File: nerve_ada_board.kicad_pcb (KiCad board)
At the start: 4 copper layers, 120 x 120 mm, 64 parts, among them J10 CAN1, J11 CAN2, J2 TC2050-IDC, J3 2171750001, J5 WS2812B, J6 Camera, J7 PA4-7, J8 PC1-3, J9 PB4-5, SW1 SPST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

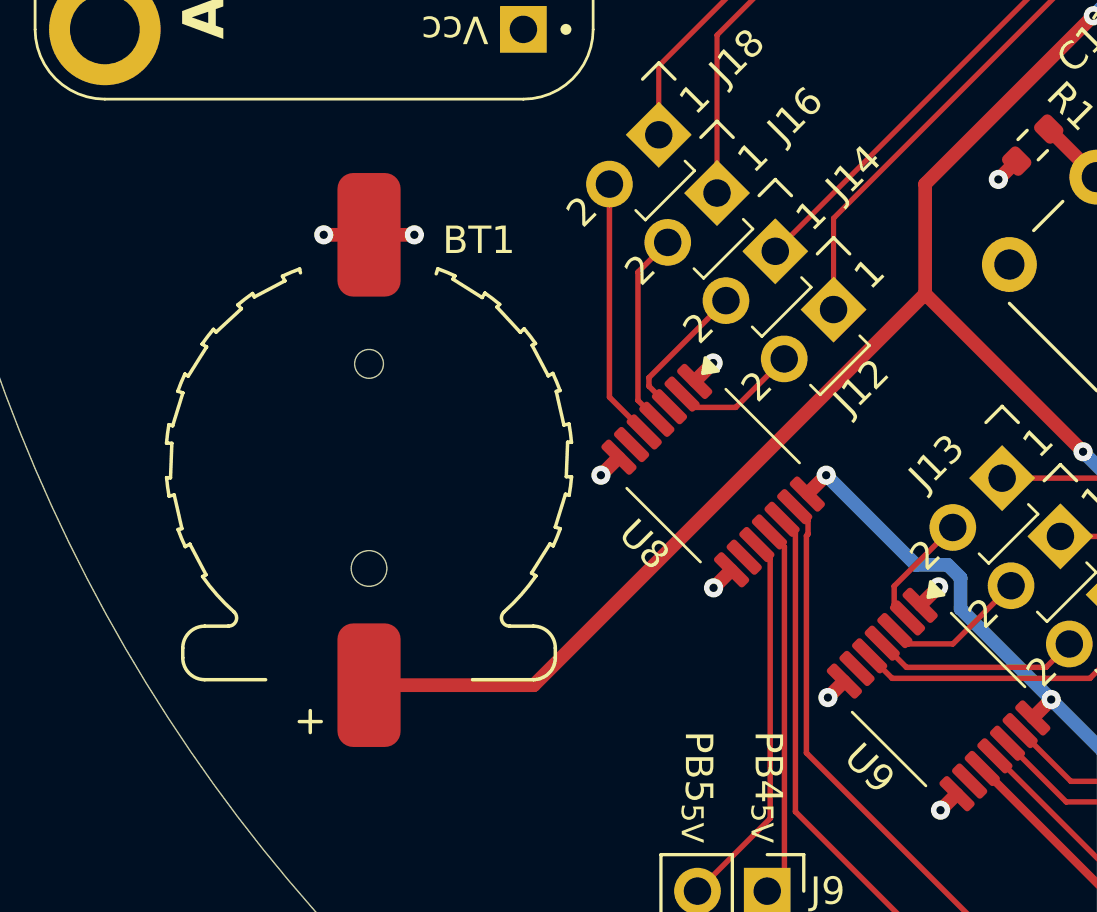
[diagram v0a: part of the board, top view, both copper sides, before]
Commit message: Update CR1220 battery holder component
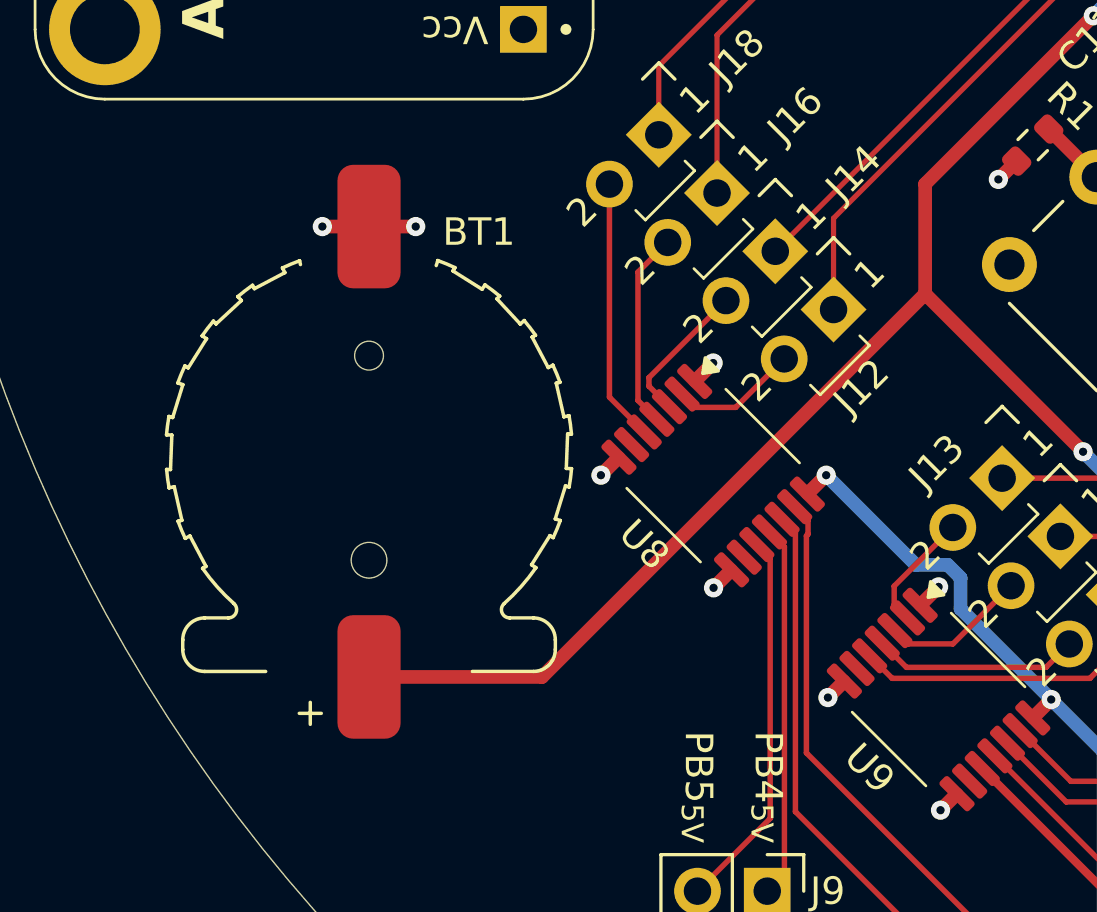
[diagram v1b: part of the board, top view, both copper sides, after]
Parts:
- BT1: footprint common:harwin_s8411-45r_cr1220_coin_battery_cell -> common:harwin_s8411-45r_cr1220
- moved BT1 0.30 mm to (105.5, 128.0)

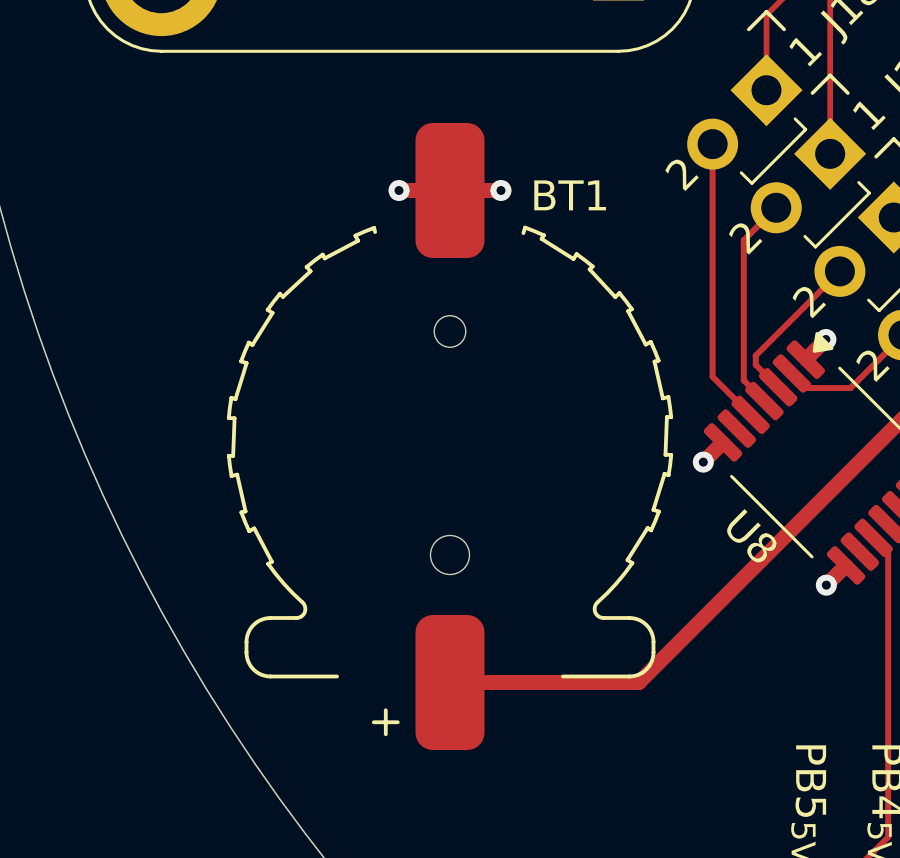
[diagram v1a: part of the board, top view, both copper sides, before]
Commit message: Update CR1220 component, again
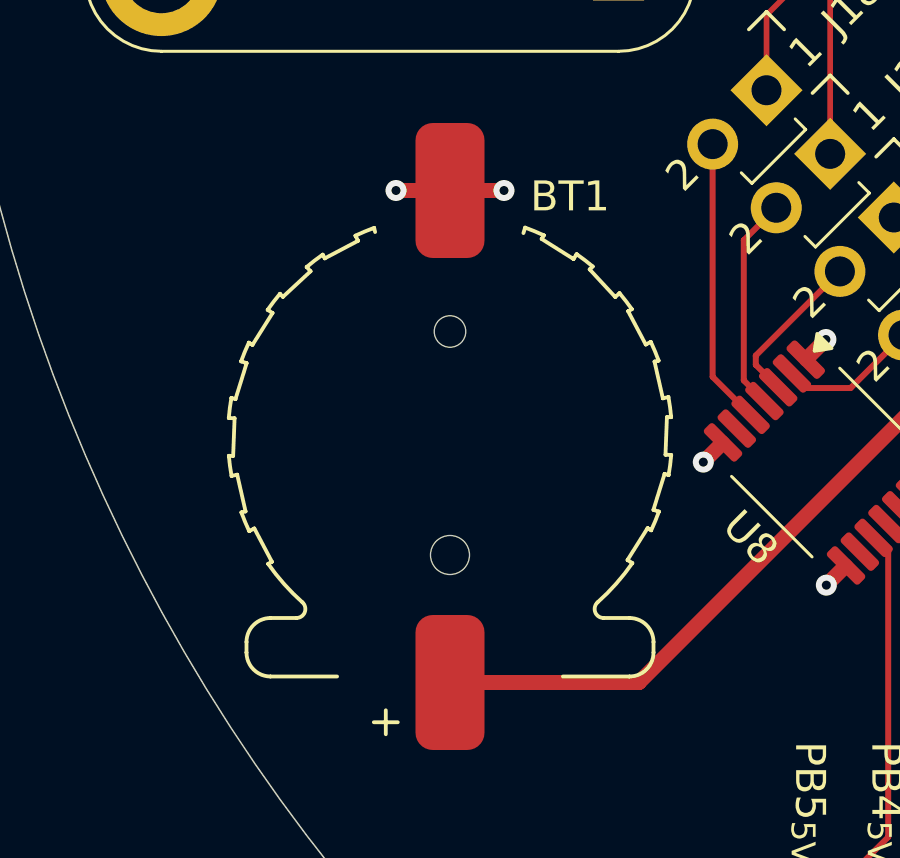
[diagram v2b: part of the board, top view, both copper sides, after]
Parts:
- BT1: footprint common:harwin_s8411-45r_cr1220 -> common:harwin_s8411-45r_cr1220_battery
